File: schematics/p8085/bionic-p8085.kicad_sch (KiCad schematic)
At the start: 8 parts, among them J1 Bionic-P135, J2 Bionic-P245, U1 P8085AH, U2 11AA010-I/TT

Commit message: [P8085] Cleanup schematics
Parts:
- D1: footprint 0-LocalLibrary:LED_CSL1901UW1_ROM-M -> rhom:LED_CSL1901UW1_ROM-M; symbol 0-LocalLibrary:CSL1901UW1 -> rhom:CSL1901UW1
- J1: footprint 0-LocalLibrary:Bionic-P135_Vertical -> bionic:Bionic-P135_Vertical; symbol 0-LocalLibrary:Bionic-P135 -> bionic:Bionic-P135
- J2: footprint 0-LocalLibrary:Bionic-P245_Vertical -> bionic:Bionic-P245_Vertical; symbol 0-LocalLibrary:Bionic-P245 -> bionic:Bionic-P245
- U1: footprint 0-LocalLibrary:DIP-40_W15.24mm_Socket -> bionic:DIP-40_W15.24mm_Socket; symbol 0-LocalLibrary:P8085AH -> cpu:P8085AH
- U2: footprint 0-LocalLibrary:SOT-23_MC_MCH-M -> microchip:SOT-23_MC_MCH-M; symbol 0-LocalLibrary:11AA010-I_TT -> microchip:11AA010-I_TT
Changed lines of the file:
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@@
 	)
 	(bus_entry
-		(at 74.93 91.44)
+		(at 67.31 83.82)
 		(size 2.54 2.54)
 		(stroke
@@
 	)
 	(bus_entry
-		(at 67.31 83.82)
+		(at 67.31 91.44)
 		(size 2.54 2.54)
 		(stroke
@@
 		)
 	)
-	(wire
-		(pts
-			(xy 77.47 93.98) (xy 85.09 93.98)
-		)
-		(stroke
-			(width 0)
-			(type default)
-		)
-	)
 	(bus
 		(pts
@@
 	(bus
 		(pts
-			(xy 74.93 96.52) (xy 74.93 91.44)
-		)
-		(stroke
-			(width 0)
-			(type default)
-		)
-	)
-	(bus
-		(pts
 			(xy 123.19 121.92) (xy 123.19 124.46)
 		)
@@
 	(bus
 		(pts
-			(xy 74.93 91.44) (xy 74.93 88.9)
+			(xy 74.93 88.9) (xy 74.93 96.52)
 		)
 		(stroke
@@
 		)
 	)
+	(wire
+		(pts
+			(xy 69.85 93.98) (xy 85.09 93.98)
+		)
+		(stroke
+			(width 0)
+			(type default)
+		)
+	)
 	(bus
 		(pts
@@
 	(bus
 		(pts
+			(xy 67.31 91.44) (xy 67.31 83.82)
+		)
+		(stroke
+			(width 0)
+			(type default)
+		)
+	)
+	(bus
+		(pts
 			(xy 123.19 127) (xy 123.19 132.08)
 		)
@@
 	(bus
 		(pts
-			(xy 67.31 97.79) (xy 67.31 83.82)
+			(xy 67.31 97.79) (xy 67.31 91.44)
 		)
 		(stroke
@@
 	)
 	(symbol
-		(lib_id "0-LocalLibrary:CSL1901UW1")
+		(lib_id "rhom:CSL1901UW1")
 		(at 208.28 38.1 270)
 		(unit 1)
@@
 		(fields_autoplaced yes)
 		(property "Reference" "D1"
-			(at 212.725 40.513 90)
+			(at 212.09 40.5129 90)
 			(effects
 				(font
@@
 		)
 		(property "Value" "CSL1901UW1"
-			(at 212.725 43.053 90)
+			(at 212.09 43.0529 90)
 			(effects
 				(font
@@
 			)
 		)
-		(property "Footprint" "0-LocalLibrary:LED_CSL1901UW1_ROM-M"
+		(property "Footprint" "rhom:LED_CSL1901UW1_ROM-M"
 			(at 199.39 41.91 0)
 			(effects
@@
 	)
 	(symbol
-		(lib_id "0-LocalLibrary:Bionic-P245")
+		(lib_id "bionic:Bionic-P245")
 		(at 171.45 104.14 0)
 		(unit 1)
@@
 			)
 		)
-		(property "Footprint" "0-LocalLibrary:Bionic-P245_Vertical"
+		(property "Footprint" "bionic:Bionic-P245_Vertical"
 			(at 172.72 139.7 0)
 			(effects
@@
 			)
 		)
-		(property "Description" ""
+		(property "Description" "Generic connector, single row, 01x24, script generated (kicad-library-utils/schlib/autogen/connector/)"
 			(at 171.45 104.14 0)
 			(effects
@@
 	)
 	(symbol
-		(lib_id "0-LocalLibrary:Bionic-P135")
+		(lib_id "bionic:Bionic-P135")
 		(at 163.83 104.14 0)
 		(unit 1)
@@
 			)
 		)
-		(property "Footprint" "0-LocalLibrary:Bionic-P135_Vertical"
+		(property "Footprint" "bionic:Bionic-P135_Vertical"
 			(at 165.1 139.7 0)
 			(effects
@@
 			)
 		)
-		(property "Description" ""
+		(property "Description" "Generic connector, single row, 01x24, script generated (kicad-library-utils/schlib/autogen/connector/)"
 			(at 163.83 104.14 0)
 			(effects
@@
 	)
 	(symbol
-		(lib_id "0-LocalLibrary:P8085AH")
+		(lib_id "cpu:P8085AH")
 		(at 96.52 106.68 0)
 		(unit 1)
@@
 			)
 		)
-		(property "Footprint" "0-LocalLibrary:DIP-40_W15.24mm_Socket"
+		(property "Footprint" "bionic:DIP-40_W15.24mm_Socket"
 			(at 97.79 140.97 0)
 			(effects
@@
 			)
 		)
-		(property "Description" ""
+		(property "Description" "8-bit General Purpose Microprocessor, DIP-40"
 			(at 96.52 106.68 0)
 			(effects
@@
 	)
 	(symbol
-		(lib_id "0-LocalLibrary:11AA010-I_TT")
+		(lib_id "microchip:11AA010-I_TT")
 		(at 198.12 77.47 0)
 		(unit 1)
@@
 			)
 		)
-		(property "Footprint" "0-LocalLibrary:SOT-23_MC_MCH-M"
+		(property "Footprint" "microchip:SOT-23_MC_MCH-M"
 			(at 200.66 95.25 0)
 			(effects
@@
 			)
 		)
-		(property "Description" ""
+		(property "Description" "UNI/O Serial EEPROM (1Kbit)"
 			(at 198.12 77.47 0)
 			(effects

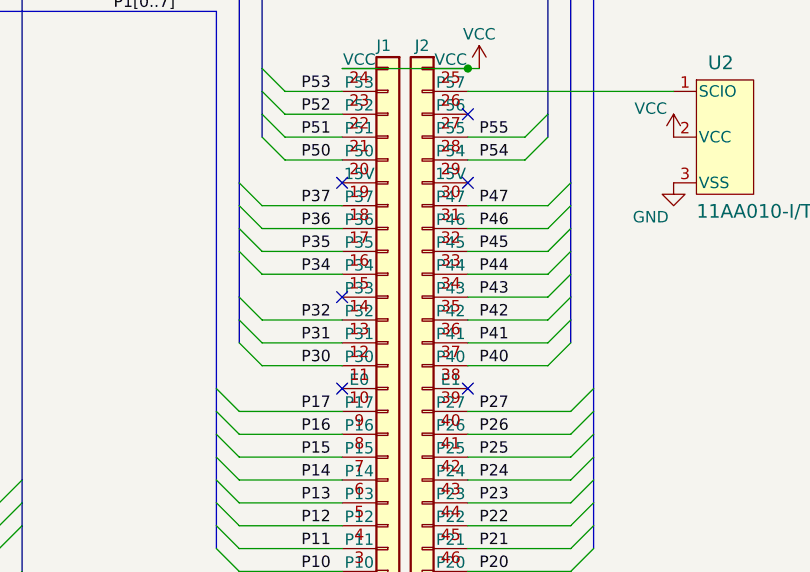
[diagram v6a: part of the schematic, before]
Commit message: [P8085] Update schematics
Remove unused pins from bionic connector
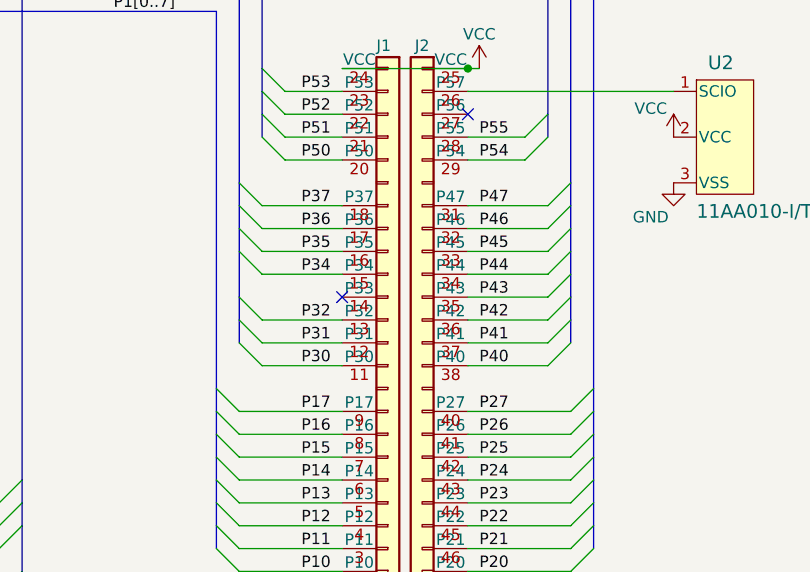
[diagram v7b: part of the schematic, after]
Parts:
- J1: footprint bionic:Bionic-P135_Vertical -> bionic:Bionic-P135_THT
- J2: footprint bionic:Bionic-P245_Vertical -> bionic:Bionic-P245_THT
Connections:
- no-connect marks 7 -> 3
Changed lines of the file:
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@@
 	(title_block
 		(title "BionicP8085")
-		(date "2024-12-02")
-		(rev "6")
+		(date "2025-03-02")
+		(rev "7")
 		(company "Tadashi G. Takaoka")
 	)
@@
 	)
 	(no_connect
-		(at 172.72 111.76)
-	)
-	(no_connect
-		(at 172.72 88.9)
-	)
-	(no_connect
 		(at 172.72 81.28)
 	)
@@
 	)
 	(no_connect
-		(at 158.75 111.76)
-	)
-	(no_connect
 		(at 85.09 127)
 	)
-	(no_connect
-		(at 158.75 88.9)
-	)
 	(bus_entry
 		(at 67.31 74.93)
@@
 			)
 		)
-		(property "Footprint" "bionic:Bionic-P245_Vertical"
+		(property "Footprint" "bionic:Bionic-P245_THT"
 			(at 172.72 139.7 0)
 			(effects
@@
 		(pin "37"
 		)
-		(pin "39"
-		)
 		(pin "38"
 		)
@@
 		(pin "29"
 		)
-		(pin "30"
-		)
 		(pin "31"
 		)
@@
 			)
 		)
-		(property "Footprint" "bionic:Bionic-P135_Vertical"
+		(property "Footprint" "bionic:Bionic-P135_THT"
 			(at 165.1 139.7 0)
 			(effects
@@
 		(pin "18"
 		)
-		(pin "10"
-		)
 		(pin "1"
 		)
@@
 		(pin "20"
 		)
-		(pin "19"
-		)
 		(pin "8"
